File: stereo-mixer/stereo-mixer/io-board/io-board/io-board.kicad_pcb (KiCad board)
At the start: 2 copper layers, 177.8 x 83.8 mm, 31 parts, among them J1 ST OUT, J10 BUS A BOARD, J11 CH B IN: L G R, J12 CH B L GAIN: TWX, J13 CH B R GAIN: TWX, J14 CH B L Level: A W B, J15 CH B R Level: A W B, J16 CH B PREAMP, J17 BUS B OUT, J18 BUS B BOARD, J19 CH C IN: L G R, J2 MIXER BOARD, J20 CH C L GAIN: TWX, J21 CH C R GAIN: TWX, J22 CH C L Level: A W B, J23 CH C R Level: A W B, J24 CH C PREAMP, J25 CH D IN: L G R, J26 CH D L GAIN: TWX, J27 CH D R GAIN: TWX, J28 CH D L Level: A W B, J29 CH D R Level: A W B, J3 CH A IN: L G R, J30 CH D PREAMP, J31 -15V GND +15V, J4 CH A L GAIN: TWX, J5 CH A R GAIN: TWX, J6 CH A L Level: A W B, J7 CH A R Level: A W B, J8 CH A PREAMP, J9 BUS A OUT

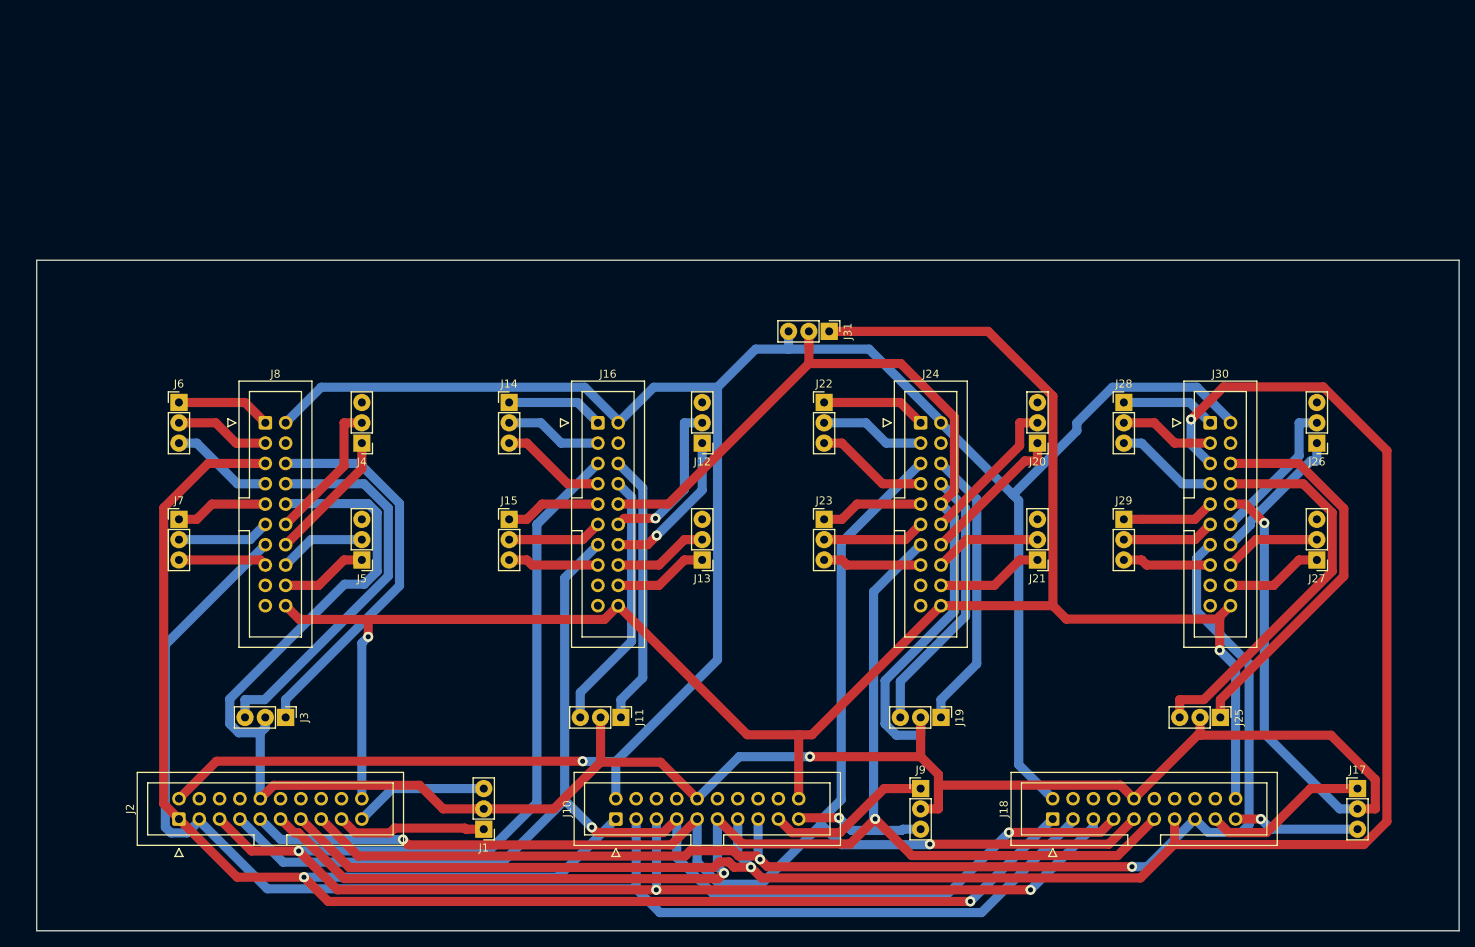
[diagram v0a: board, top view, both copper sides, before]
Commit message: minor adjustment to I/O board layout to avoid board edge
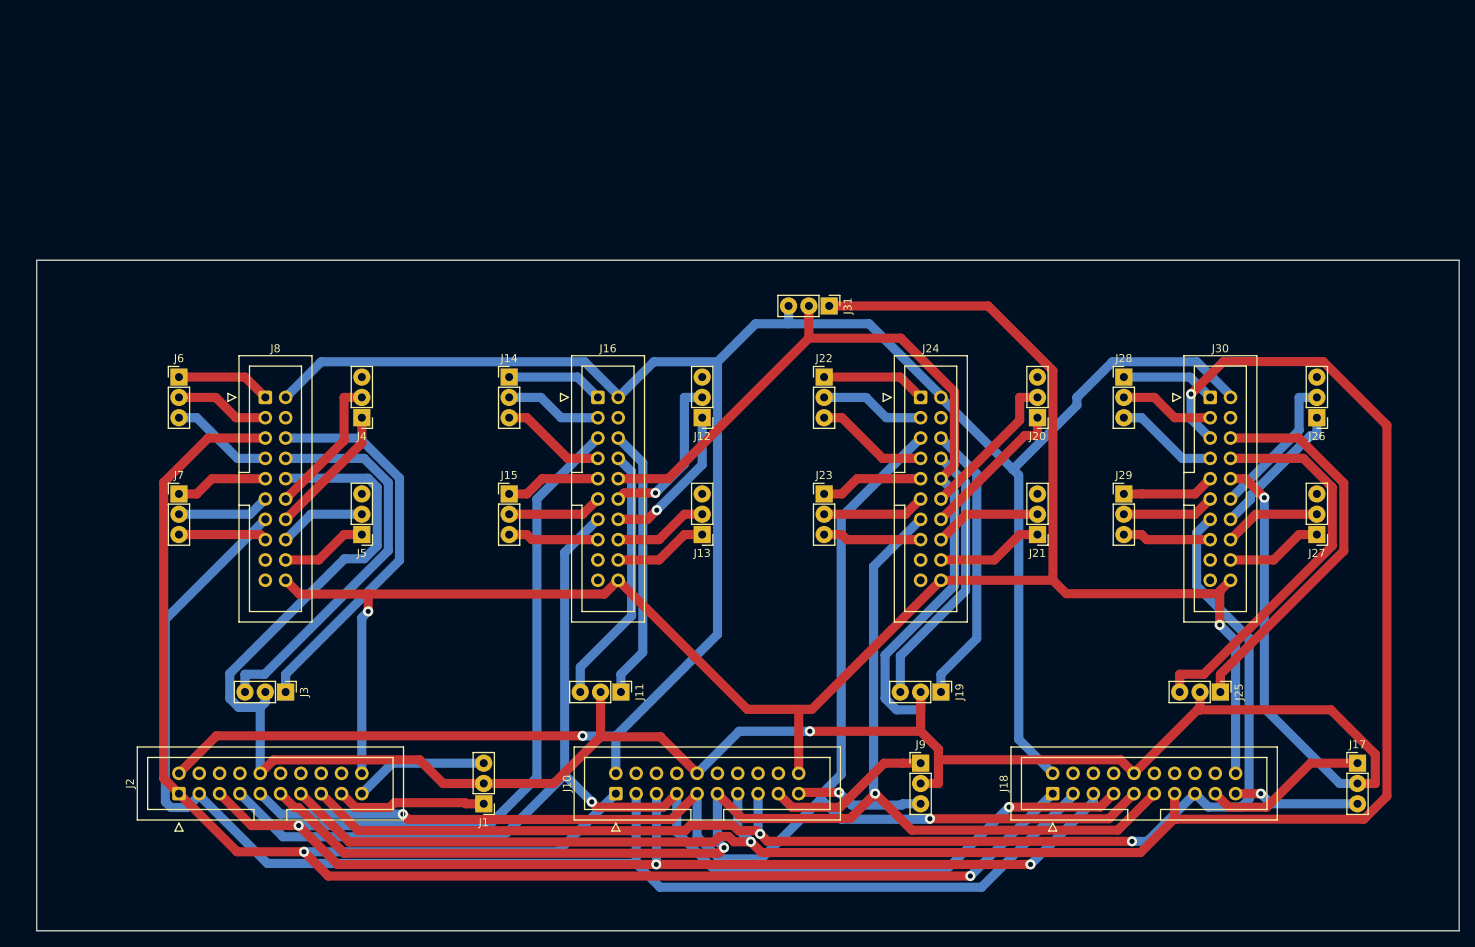
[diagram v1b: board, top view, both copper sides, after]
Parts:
- moved J1 3.18 mm to (109.2, 117.5)
- moved J11 3.18 mm to (126.4, 103.5)
- moved J13 3.18 mm to (136.5, 83.8)
- moved J15 3.18 mm to (112.4, 78.7)
- moved J19 3.18 mm to (166.4, 103.5)
- moved J21 3.18 mm to (178.4, 83.8)
- moved J23 3.18 mm to (151.8, 78.7)
- moved J25 3.18 mm to (201.3, 103.5)
- moved J27 3.18 mm to (213.4, 83.8)
- moved J29 3.18 mm to (189.2, 78.7)
- moved J3 3.18 mm to (84.5, 103.5)
- moved J5 3.18 mm to (94.0, 83.8)
- moved J7 3.18 mm to (71.1, 78.7)
- moved J31 3.18 mm to (152.4, 55.2)
- moved J10 3.17 mm to (125.7, 116.2)
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
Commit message: added labels and fill areas to I/O board
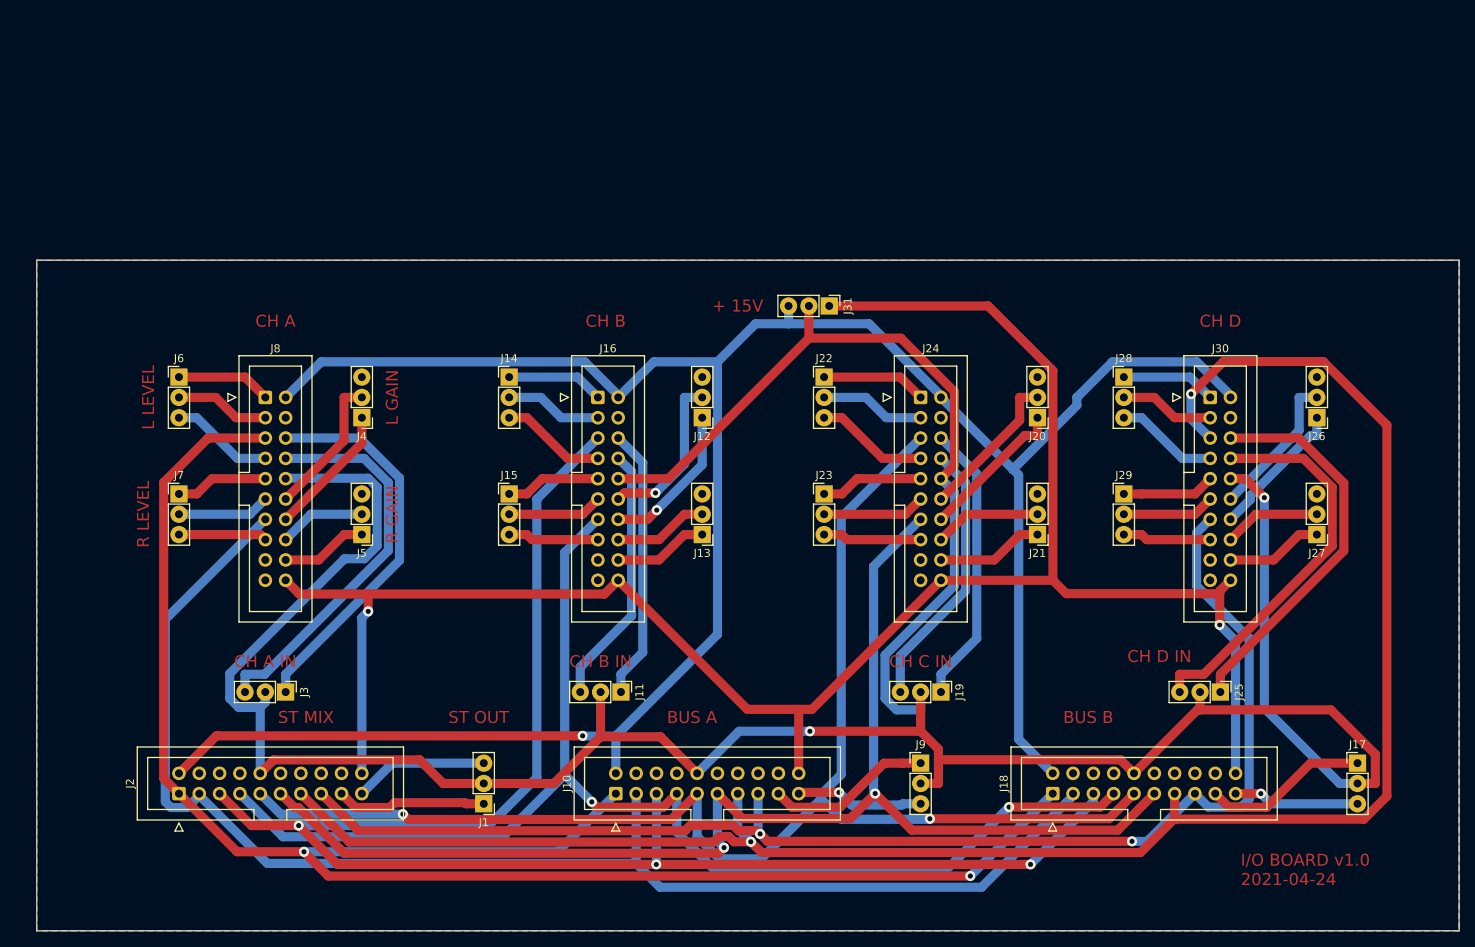
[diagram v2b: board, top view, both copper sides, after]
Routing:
- added copper zone on B.Cu, net (none)
- added copper zone on F.Cu, net (none)
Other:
- board text added: "+ 15V"
- board text added: "BUS A"
- board text added: "BUS B"
- board text added: "CH A"
- board text added: "CH A IN"
- board text added: "CH B"
- board text added: "CH B IN"
- board text added: "CH C IN"
- board text added: "CH D"
- board text added: "CH D IN"
- board text added: "I/O BOARD v1.0 2021-04-24"
- board text added: "L GAIN"
- board text added: "L LEVEL"
- board text added: "R GAIN"
- board text added: "R LEVEL"
- board text added: "ST MIX"
- board text added: "ST OUT"
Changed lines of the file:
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@@
   (general
     (thickness 1.6)
-    (drawings 9)
+    (drawings 31)
     (tracks 442)
     (zones 0)
@@
   (layers
     (0 F.Cu signal)
-    (31 B.Cu signal)
+    (31 B.Cu signal hide)
     (32 B.Adhes user)
     (33 F.Adhes user)
@@
     )
   )
+  (gr_text "+ 15V" (at 140.97 55.245) (layer F.Cu)
+    (effects (font (size 1.5 1.5) (thickness 0.3)))
+  )
+  (gr_text "CH D IN" (at 193.675 99.06) (layer F.Cu)
+    (effects (font (size 1.5 1.5) (thickness 0.3)))
+  )
+  (gr_text "BUS B" (at 184.785 106.68) (layer F.Cu)
+    (effects (font (size 1.5 1.5) (thickness 0.3)))
+  )
+  (gr_text "BUS A" (at 135.255 106.68) (layer F.Cu)
+    (effects (font (size 1.5 1.5) (thickness 0.3)))
+  )
+  (gr_text "ST OUT" (at 108.585 106.68) (layer F.Cu)
+    (effects (font (size 1.5 1.5) (thickness 0.3)))
+  )
+  (gr_text "ST MIX" (at 86.995 106.68) (layer F.Cu)
+    (effects (font (size 1.5 1.5) (thickness 0.3)))
+  )
+  (gr_text "CH C IN" (at 163.83 99.695) (layer F.Cu)
+    (effects (font (size 1.5 1.5) (thickness 0.3)))
+  )
+  (gr_text "CH B IN" (at 123.825 99.695) (layer F.Cu)
+    (effects (font (size 1.5 1.5) (thickness 0.3)))
+  )
+  (gr_text "CH A IN" (at 81.915 99.695) (layer F.Cu)
+    (effects (font (size 1.5 1.5) (thickness 0.3)))
+  )
+  (gr_text "R GAIN" (at 97.79 81.28 90) (layer F.Cu)
+    (effects (font (size 1.5 1.5) (thickness 0.3)))
+  )
+  (gr_text "L GAIN" (at 97.79 66.675 90) (layer F.Cu)
+    (effects (font (size 1.5 1.5) (thickness 0.3)))
+  )
+  (gr_text "R LEVEL" (at 66.675 81.28 90) (layer F.Cu)
+    (effects (font (size 1.5 1.5) (thickness 0.3)))
+  )
+  (gr_text "L LEVEL" (at 67.31 66.675 90) (layer F.Cu)
+    (effects (font (size 1.5 1.5) (thickness 0.3)))
+  )
+  (gr_text "CH D" (at 201.295 57.15) (layer F.Cu)
+    (effects (font (size 1.5 1.5) (thickness 0.3)))
+  )
+  (gr_text "CH B" (at 124.46 57.15) (layer F.Cu)
+    (effects (font (size 1.5 1.5) (thickness 0.3)))
+  )
+  (gr_text "CH A" (at 83.185 57.15) (layer F.Cu)
+    (effects (font (size 1.5 1.5) (thickness 0.3)))
+  )
+  (gr_text "I/O BOARD v1.0\n2021-04-24" (at 203.835 125.73) (layer F.Cu)
+    (effects (font (size 1.5 1.5) (thickness 0.3)) (justify left))
+  )
+  (target plus (at 71.755 125.095) (size 5) (width 0.05) (layer Edge.Cuts))
+  (target plus (at 190.5 56.515) (size 5) (width 0.05) (layer Edge.Cuts))
+  (target plus (at 200.66 125.73) (size 5) (width 0.05) (layer Edge.Cuts))
+  (target plus (at 133.985 55.245) (size 5) (width 0.05) (layer Edge.Cuts))
+  (target plus (at 62.23 58.42) (size 5) (width 0.254) (layer Edge.Cuts))
   (dimension 36.200006 (width 0.15) (layer Dwgs.User)
     (gr_text "1.4252 in" (at 200.968055 39.330007 0.03165512358) (layer Dwgs.User)
@@
   (segment (start 200.025 84.455) (end 192.0875 84.455) (width 1.143) (layer F.Cu) (net 85))
   (segment (start 192.0875 84.455) (end 191.4525 83.82) (width 1.143) (layer F.Cu) (net 85))
+  (zone (net 0) (net_name "") (layer F.Cu) (hatch edge 0.508)
+    (connect_pads (clearance 0.508))
+    (min_thickness 0.254)
+    (fill yes (arc_segments 32) (thermal_gap 0.508) (thermal_bridge_width 0.508))
+    (polygon
+      (pts
+        (xy 231.14 133.35) (xy 53.34 133.35) (xy 53.34 49.53) (xy 231.14 49.53)
+      )
+    )
+  )
+  (zone (net 0) (net_name "") (layer B.Cu) (hatch edge 0.508)
+    (connect_pads (clearance 0.508))
+    (min_thickness 0.254)
+    (fill yes (arc_segments 32) (thermal_gap 0.508) (thermal_bridge_width 0.508))
+    (polygon
+      (pts
+        (xy 231.14 133.35) (xy 53.34 133.35) (xy 53.34 49.53) (xy 231.14 49.53)
+      )
+    )
+  )
 )

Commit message: updated after print and etch
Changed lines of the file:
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@@
   (layers
     (0 F.Cu signal)
-    (31 B.Cu signal hide)
+    (31 B.Cu signal)
     (32 B.Adhes user)
     (33 F.Adhes user)
@@
     (38 B.Mask user)
     (39 F.Mask user)
-    (40 Dwgs.User user hide)
+    (40 Dwgs.User user)
     (41 Cmts.User user)
     (42 Eco1.User user)
@@
     )
   )
+  (gr_circle (center 62.23 58.42) (end 65.405 58.42) (layer F.Cu) (width 0.15))
   (gr_text "+ 15V" (at 140.97 55.245) (layer F.Cu)
     (effects (font (size 1.5 1.5) (thickness 0.3)))
@@
     (effects (font (size 1.5 1.5) (thickness 0.3)) (justify left))
   )
-  (target plus (at 71.755 125.095) (size 5) (width 0.05) (layer Edge.Cuts))
+  (target plus (at 71.755 125.095) (size 5) (width 0.254) (layer Edge.Cuts))
   (target plus (at 190.5 56.515) (size 5) (width 0.05) (layer Edge.Cuts))
-  (target plus (at 200.66 125.73) (size 5) (width 0.05) (layer Edge.Cuts))
-  (target plus (at 133.985 55.245) (size 5) (width 0.05) (layer Edge.Cuts))
+  (target plus (at 200.66 125.73) (size 5) (width 0.254) (layer Edge.Cuts))
+  (target plus (at 133.985 55.245) (size 5) (width 0.254) (layer Edge.Cuts))
   (target plus (at 62.23 58.42) (size 5) (width 0.254) (layer Edge.Cuts))
   (dimension 36.200006 (width 0.15) (layer Dwgs.User)
@@
   (gr_line (start 53.34 133.35) (end 231.14 133.35) (layer Edge.Cuts) (width 0.05))
   (gr_line (start 53.34 49.53) (end 53.34 133.35) (layer Dwgs.User) (width 0.15))
-  (gr_line (start 233.68 55.88) (end 55.88 55.88) (layer Dwgs.User) (width 0.15))
   (gr_line (start 231.14 133.35) (end 231.14 49.53) (layer Dwgs.User) (width 0.15))
   (gr_line (start 53.34 133.35) (end 231.14 133.35) (layer Dwgs.User) (width 0.15))
@@
       )
     )
+  )
+  (zone (net 0) (net_name "") (layers F&B.Cu) (hatch edge 0.508)
+    (connect_pads (clearance 0.508))
+    (min_thickness 0.254)
+    (keepout (tracks not_allowed) (vias not_allowed) (copperpour not_allowed))
+    (fill (arc_segments 32) (thermal_gap 0.508) (thermal_bridge_width 0.508))
+    (polygon
+      (pts
+        (xy 64.77 60.96) (xy 59.69 60.96) (xy 59.69 55.88) (xy 64.77 55.88)
+      )
+    )
+  )
+  (zone (net 0) (net_name "") (layers F&B.Cu) (hatch edge 0.508)
+    (connect_pads (clearance 0.508))
+    (min_thickness 0.254)
+    (keepout (tracks not_allowed) (vias not_allowed) (copperpour allowed))
+    (fill (arc_segments 32) (thermal_gap 0.508) (thermal_bridge_width 0.508))
+    (polygon
+      (pts
+        (xy 193.04 59.055) (xy 187.96 59.055) (xy 187.96 53.975) (xy 193.04 53.975)
+      )
+    )
+  )
+  (zone (net 0) (net_name "") (layers F&B.Cu) (hatch edge 0.508)
+    (connect_pads (clearance 0.508))
+    (min_thickness 0.254)
+    (keepout (tracks not_allowed) (vias not_allowed) (copperpour not_allowed))
+    (fill (arc_segments 32) (thermal_gap 0.508) (thermal_bridge_width 0.508))
+    (polygon
+      (pts
+        (xy 193.04 59.055) (xy 187.96 59.055) (xy 187.96 53.975) (xy 193.04 53.975)
+      )
+    )
+  )
+  (zone (net 0) (net_name "") (layers F&B.Cu) (hatch edge 0.508)
+    (connect_pads (clearance 0.508))
+    (min_thickness 0.254)
+    (keepout (tracks not_allowed) (vias not_allowed) (copperpour not_allowed))
+    (fill (arc_segments 32) (thermal_gap 0.508) (thermal_bridge_width 0.508))
+    (polygon
+      (pts
+        (xy 203.2 128.27) (xy 198.12 128.27) (xy 198.12 123.19) (xy 203.2 123.19)
+      )
+    )
+  )
+  (zone (net 0) (net_name "") (layers F&B.Cu) (hatch edge 0.508)
+    (connect_pads (clearance 0.508))
+    (min_thickness 0.254)
+    (keepout (tracks not_allowed) (vias not_allowed) (copperpour not_allowed))
+    (fill (arc_segments 32) (thermal_gap 0.508) (thermal_bridge_width 0.508))
+    (polygon
+      (pts
+        (xy 74.295 127.635) (xy 69.215 127.635) (xy 69.215 122.555) (xy 74.295 122.555)
+      )
+    )
+  )
+  (zone (net 0) (net_name "") (layers F&B.Cu) (hatch edge 0.508)
+    (connect_pads (clearance 0.508))
+    (min_thickness 0.254)
+    (keepout (tracks not_allowed) (vias not_allowed) (copperpour not_allowed))
+    (fill (arc_segments 32) (thermal_gap 0.508) (thermal_bridge_width 0.508))
+    (polygon
+      (pts
+        (xy 136.525 57.785) (xy 131.445 57.785) (xy 131.445 52.705) (xy 136.525 52.705)
+      )
+    )

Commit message: updated for cnc
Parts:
- moved J31 66.8 mm to (212.7, 83.8), turned to 90 degrees
- moved Jr 32.6 mm to (64.1, 39.4), turned to 90 degrees
- moved J16 32.1 mm to (106.7, 39.4), turned to 90 degrees
- moved J24 31.0 mm to (149.2, 39.4), turned to 90 degrees
- moved J11 29.7 mm to (104.1, 83.8), turned to 90 degrees
- moved J30 28.3 mm to (192.4, 39.4), turned to 90 degrees
- moved J19 27.8 mm to (146.7, 83.8), turned to 90 degrees
- moved J3 25.3 mm to (68.6, 83.8)
- moved J25 22.8 mm to (189.9, 83.8), turned to 90 degrees
- moved J1 18.1 mm to (103.5, 100.3)
- moved J10 18.1 mm to (120.0, 99.1)
- moved J18 18.1 mm to (174.6, 99.1)
- moved J2 18.1 mm to (65.4, 99.1)
- moved J9 18.1 mm to (158.1, 95.2)
- moved J17 17.6 mm to (214.6, 95.2)
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- renumbered J8 to Jr
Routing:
- net /-_15V: track 246.0 -> 370.2 mm
- net GND: track 396.0 -> 486.5 mm, vias 2 -> 0
- net /+_15V: track 297.0 -> 386.3 mm
- net /CH_C_R_OUT: track 163.7 -> 239.9 mm
- net /CH_B_R_IN: track 32.6 -> 93.9 mm
- net /CH_B_R_OUT: track 161.4 -> 222.6 mm, vias 2 -> 3
- net /CH_A_R_OUT: track 173.6 -> 229.5 mm, vias 0 -> 3
- net /CH_C_R_IN: track 33.9 -> 86.0 mm
- net /CH_B_R_GAIN_WIPER: track 11.8 -> 57.6 mm
- net /CH_D_R_GAIN_WIPER: track 12.1 -> 57.4 mm
- net /CH_D_R_OUT: track 166.1 -> 211.1 mm
- net /CH_A_R_GAIN_WIPER: track 10.8 -> 52.4 mm
- net /CH_A_R_GAIN_TERM_A: track 10.8 -> 51.9 mm
- net /CH_C_R_GAIN_WIPER: track 13.4 -> 53.6 mm, vias 0 -> 1
- net /CH_C_L_OUT: track 174.2 -> 213.3 mm, vias 2 -> 1
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- removed copper zone on B.Cu, net (none)
- removed copper zone on F.Cu, net (none)
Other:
- board size 177.8 x 83.8 mm -> 177.8 x 108 mm
- net class Default: clearance 0.254 -> 1; trace_width 1.143 -> 1; via_dia 0.8 -> 2; via_drill 0.4 -> 1
- rule trace_clearance: 0.254 -> 1
- board text added: "- 15V G + 15V"
- board text added: "BUS A OUT"
- board text added: "BUS B OUT"
- board text added: "CH C"
- board text added: "I/O BOARD v1.1 2021-05-02"
- board text removed: "+ 15V"
- board text removed: "I/O BOARD v1.0 2021-04-24"
